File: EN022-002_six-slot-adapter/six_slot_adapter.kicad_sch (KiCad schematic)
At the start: 17 parts, among them J3 CART SLOT TOP ROW, J4 CART SLOT BOTTOM ROW, M2_1 Screw_Terminal_01x01, M2_2 Screw_Terminal_01x01, M2_5 Screw_Terminal_01x01, M2_6 Screw_Terminal_01x01

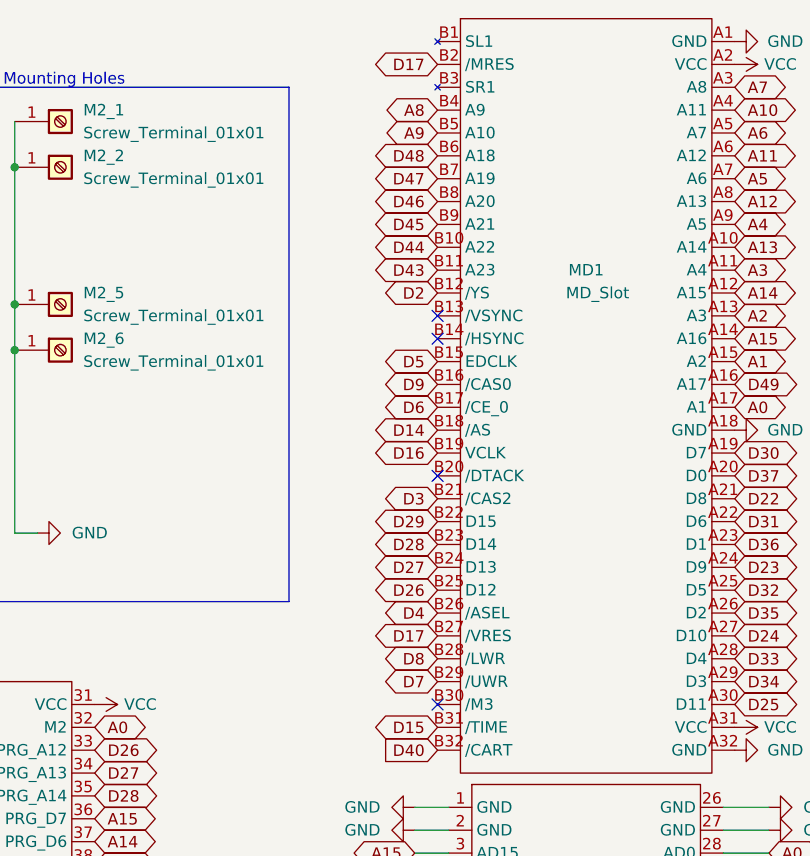
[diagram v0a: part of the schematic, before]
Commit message: first cimplete  version of CPU POWER BASE
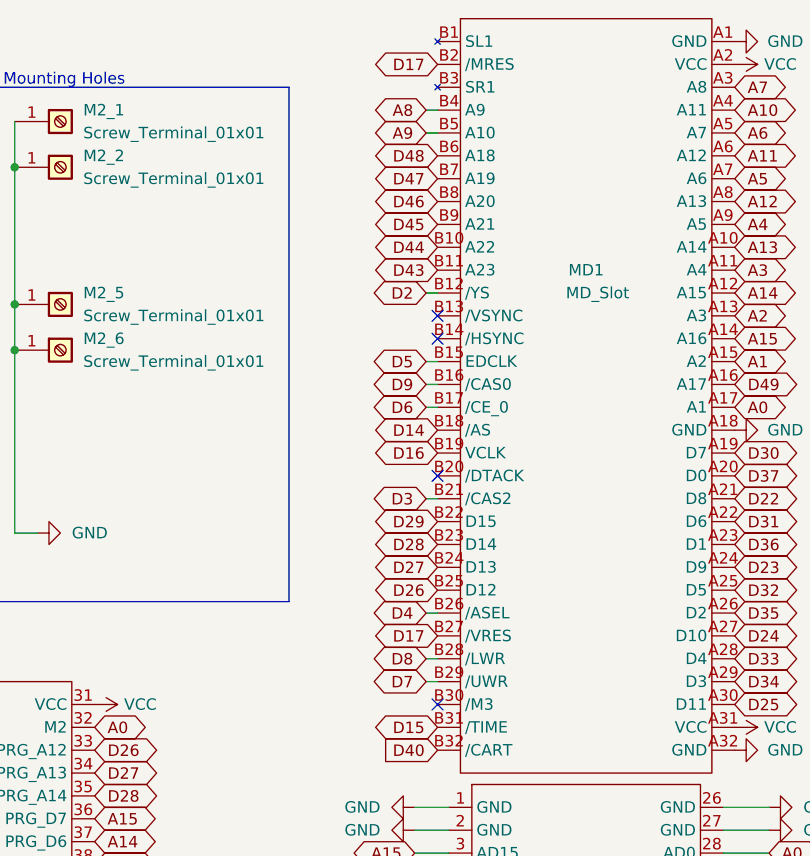
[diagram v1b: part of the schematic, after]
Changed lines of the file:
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@@
 (kicad_sch
-	(version 20231120)
+	(version 20250114)
 	(generator "eeschema")
-	(generator_version "8.0")
+	(generator_version "9.0")
 	(paper "A4")
 	(title_block
@@
 		(rev "4")
 	)
+	(text "Mounting Holes"
+		(exclude_from_sim no)
+		(at 190.5 20.32 0)
+		(effects
+			(font
+				(size 1.27 1.27)
+			)
+			(justify left bottom)
+		)
+	)
 	(junction
 		(at 191.77 49.53)
@@
 	(wire
 		(pts
+			(xy 237.49 25.4) (xy 238.76 25.4)
+		)
+		(stroke
+			(width 0)
+			(type default)
+		)
+	)
+	(wire
+		(pts
 			(xy 270.51 156.21) (xy 275.59 156.21)
 		)
@@
 	(wire
 		(pts
+			(xy 237.49 55.88) (xy 238.76 55.88)
+		)
+		(stroke
+			(width 0)
+			(type default)
+		)
+	)
+	(wire
+		(pts
 			(xy 43.18 53.34) (xy 43.18 57.15)
 		)
@@
 	(wire
 		(pts
+			(xy 237.49 22.86) (xy 238.76 22.86)
+		)
+		(stroke
+			(width 0)
+			(type default)
+		)
+	)
+	(wire
+		(pts
 			(xy 71.12 83.82) (xy 77.47 83.82)
 		)
@@
 	(wire
 		(pts
+			(xy 237.49 43.18) (xy 238.76 43.18)
+		)
+		(stroke
+			(width 0)
+			(type default)
+		)
+	)
+	(wire
+		(pts
 			(xy 63.5 53.34) (xy 63.5 57.15)
 		)
@@
 	(wire
 		(pts
+			(xy 237.49 78.74) (xy 238.76 78.74)
+		)
+		(stroke
+			(width 0)
+			(type default)
+		)
+	)
+	(wire
+		(pts
 			(xy 25.4 91.44) (xy 30.48 91.44)
 		)
@@
 	(wire
 		(pts
+			(xy 237.49 53.34) (xy 238.76 53.34)
+		)
+		(stroke
+			(width 0)
+			(type default)
+		)
+	)
+	(wire
+		(pts
+			(xy 237.49 86.36) (xy 238.76 86.36)
+		)
+		(stroke
+			(width 0)
+			(type default)
+		)
+	)
+	(wire
+		(pts
 			(xy 71.12 134.62) (xy 77.47 134.62)
 		)
@@
 	(wire
 		(pts
+			(xy 237.49 83.82) (xy 238.76 83.82)
+		)
+		(stroke
+			(width 0)
+			(type default)
+		)
+	)
+	(wire
+		(pts
 			(xy 270.51 102.87) (xy 275.59 102.87)
 		)
@@
 	(wire
 		(pts
+			(xy 237.49 66.04) (xy 238.76 66.04)
+		)
+		(stroke
+			(width 0)
+			(type default)
+		)
+	)
+	(wire
+		(pts
 			(xy 93.98 26.67) (xy 93.98 30.48)
 		)
@@
 		)
 	)
-	(text "Mounting Holes"
-		(exclude_from_sim no)
-		(at 190.5 20.32 0)
-		(effects
-			(font
-				(size 1.27 1.27)
-			)
-			(justify left bottom)
+	(wire
+		(pts
+			(xy 237.49 50.8) (xy 238.76 50.8)
+		)
+		(stroke
+			(width 0)
+			(type default)
 		)
 	)
@@
 	(global_label "A8"
 		(shape bidirectional)
-		(at 238.76 22.86 180)
+		(at 237.49 22.86 180)
 		(fields_autoplaced yes)
 		(effects
@@
 		)
 		(property "Intersheetrefs" "${INTERSHEET_REFS}"
-			(at 234.0488 22.7806 0)
+			(at 232.7788 22.7806 0)
 			(effects
 				(font
@@
 	(global_label "D8"
 		(shape bidirectional)
-		(at 238.76 83.82 180)
+		(at 237.49 83.82 180)
 		(fields_autoplaced yes)
 		(effects
@@
 		)
 		(property "Intersheetrefs" "${INTERSHEET_REFS}"
-			(at 233.8674 83.7406 0)
+			(at 232.5974 83.7406 0)
 			(effects
 				(font
@@
 	(global_label "D2"
 		(shape bidirectional)
-		(at 238.76 43.18 180)
+		(at 237.49 43.18 180)
 		(fields_autoplaced yes)
 		(effects
@@
 		)
 		(property "Intersheetrefs" "${INTERSHEET_REFS}"
-			(at 233.8674 43.1006 0)
+			(at 232.5974 43.1006 0)
 			(effects
 				(font
@@
 	(global_label "D7"
 		(shape bidirectional)
-		(at 238.76 86.36 180)
+		(at 237.49 86.36 180)
 		(fields_autoplaced yes)
 		(effects
@@
 		)
 		(property "Intersheetrefs" "${INTERSHEET_REFS}"
-			(at 233.8674 86.2806 0)
+			(at 232.5974 86.2806 0)
 			(effects
 				(font
@@
 	(global_label "D9"
 		(shape bidirectional)
-		(at 238.76 53.34 180)
+		(at 237.49 53.34 180)
 		(fields_autoplaced yes)
 		(effects
@@
 		)
 		(property "Intersheetrefs" "${INTERSHEET_REFS}"
-			(at 233.8674 53.2606 0)
+			(at 232.5974 53.2606 0)
 			(effects
 				(font
@@
 	(global_label "D4"
 		(shape bidirectional)
-		(at 238.76 78.74 180)
+		(at 237.49 78.74 180)
 		(fields_autoplaced yes)
 		(effects
@@
 		)
 		(property "Intersheetrefs" "${INTERSHEET_REFS}"
-			(at 233.8674 78.6606 0)
+			(at 232.5974 78.6606 0)
 			(effects
 				(font
@@
 	(global_label "D6"
 		(shape bidirectional)
-		(at 238.76 55.88 180)
+		(at 237.49 55.88 180)
 		(fields_autoplaced yes)
 		(effects
@@
 		)
 		(property "Intersheetrefs" "${INTERSHEET_REFS}"
-			(at 233.8674 55.8006 0)
+			(at 232.5974 55.8006 0)
 			(effects
 				(font
@@
 	(global_label "D5"
 		(shape bidirectional)
-		(at 238.76 50.8 180)
+		(at 237.49 50.8 180)
 		(fields_autoplaced yes)
 		(effects
@@
 		)
 		(property "Intersheetrefs" "${INTERSHEET_REFS}"
-			(at 233.8674 50.7206 0)
+			(at 232.5974 50.7206 0)
 			(effects
 				(font
@@
 	(global_label "A9"
 		(shape bidirectional)
-		(at 238.76 25.4 180)
+		(at 237.49 25.4 180)
 		(fields_autoplaced yes)
 		(effects
@@
 		)
 		(property "Intersheetrefs" "${INTERSHEET_REFS}"
-			(at 234.0488 25.3206 0)
+			(at 232.7788 25.3206 0)
 			(effects
 				(font
@@
 	(global_label "D3"
 		(shape bidirectional)
-		(at 238.76 66.04 180)
+		(at 237.49 66.04 180)
 		(fields_autoplaced yes)
 		(effects
@@
 		)
 		(property "Intersheetrefs" "${INTERSHEET_REFS}"
-			(at 233.8674 65.9606 0)
+			(at 232.5974 65.9606 0)
 			(effects
 				(font
@@
 		)
 	)
+	(embedded_fonts no)
 )
